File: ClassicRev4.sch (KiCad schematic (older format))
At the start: 60 parts, among them IC1 7805TV, IC2 MEGA8-P, IC3 74141N, Q1 IRF740, Q2 16MHz, Q3 2N7000, Q4 2N7000, Q5 2N7000, Q6 2N7000

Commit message: Initial commit Classic Rev4c
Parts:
- added TP4: HVD, Recovered:TESTPAD_P1-13, symbol TEST_1P
- IC3: value 74141N -> K155ID1
- SV2: footprint Recovered:ARDUNIX6_MA04-1 -> Recovered:ARDUNIX6_MA06-1; symbol ARDUNIX6_MA04-1 -> ARDUNIX6_MA06-1
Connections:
- net labels added: B_GATE, GPIO, G_GATE, PIR, R_GATE, TICK_BASE
- net labels removed: N$1, N$31, N$32, N$35, gnd
- wire segments 229 -> 231

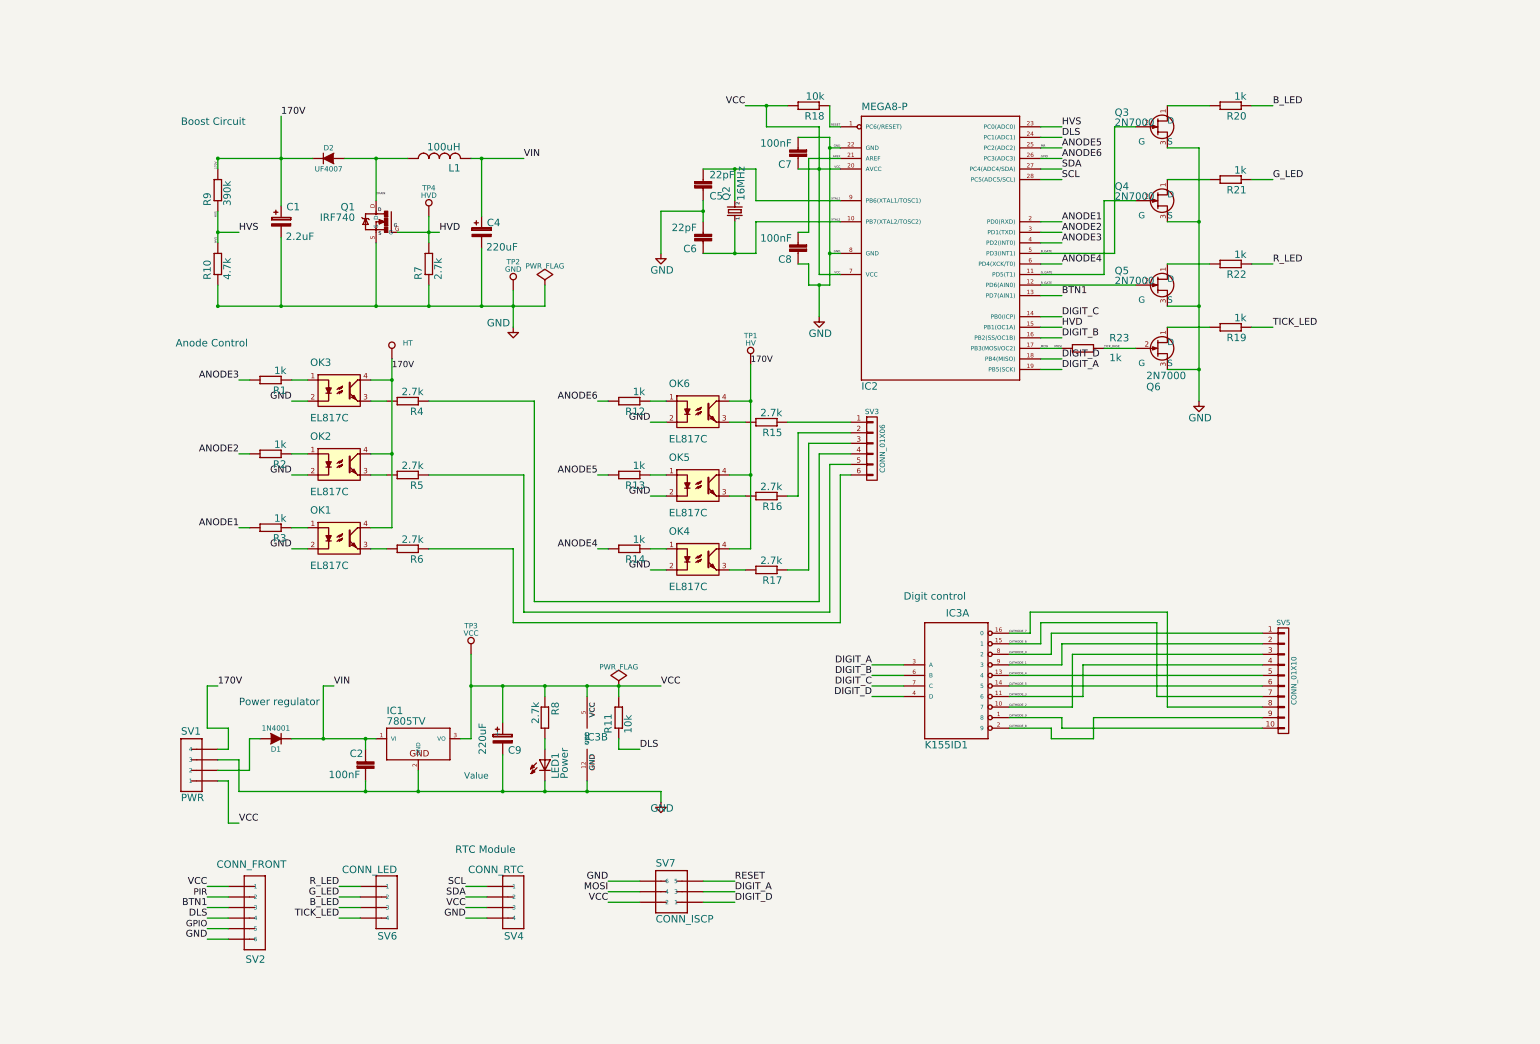
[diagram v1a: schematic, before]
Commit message: Correct values and divide more logically
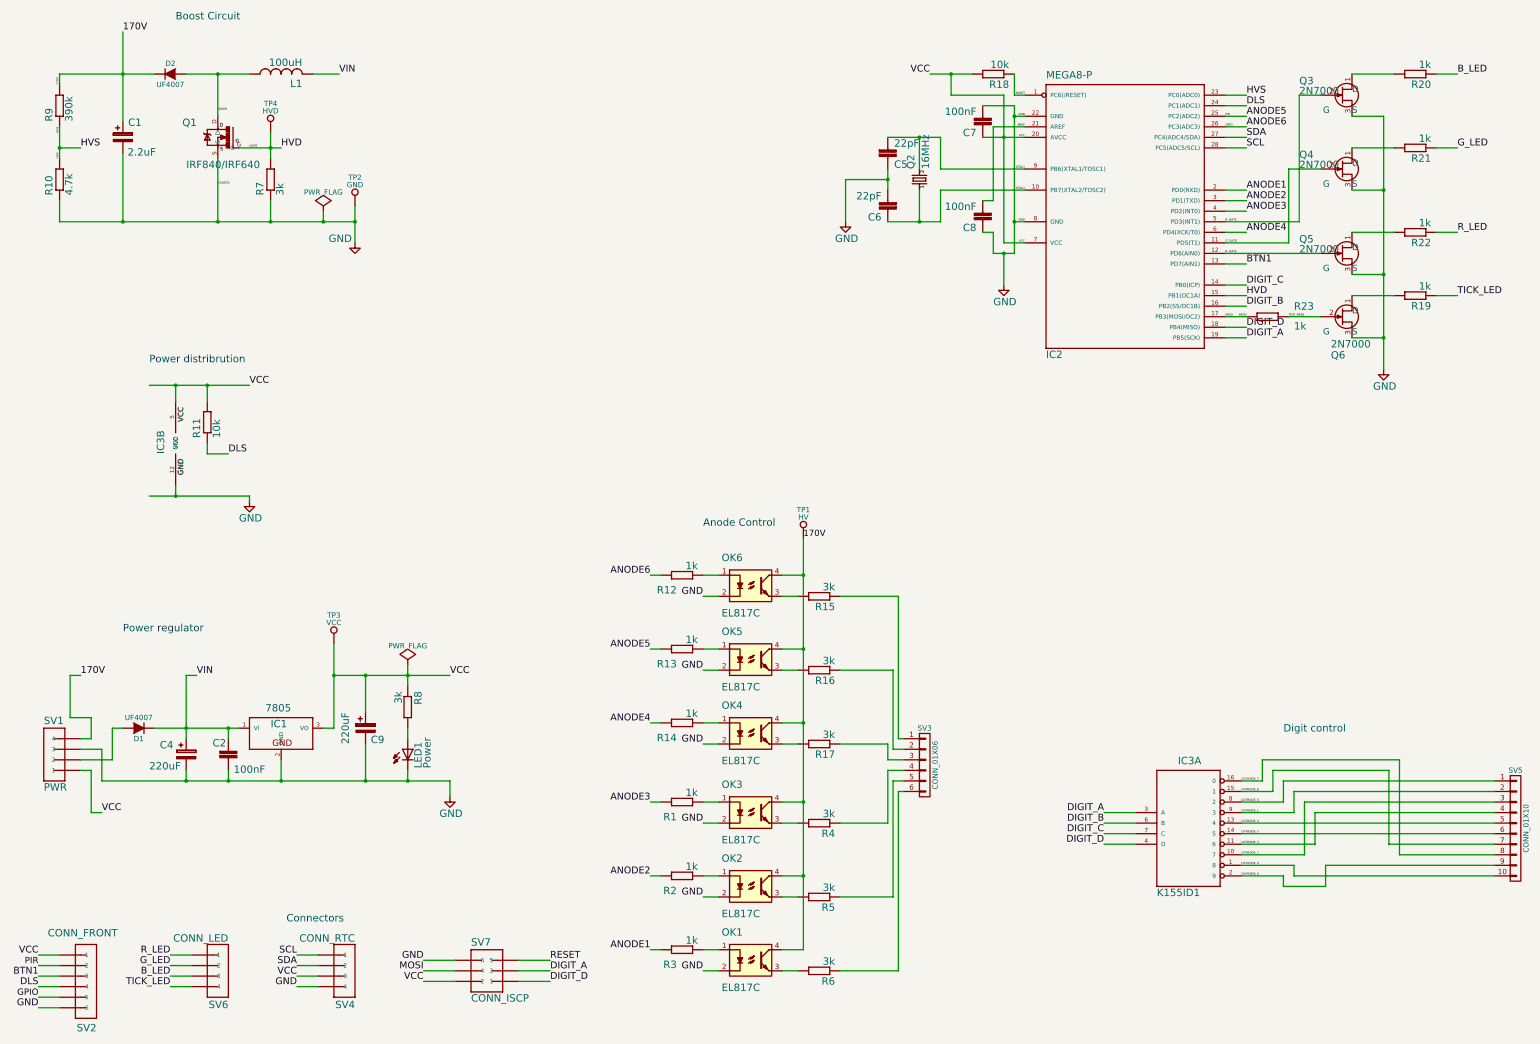
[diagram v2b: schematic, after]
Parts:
- D1: value 1N4001 -> UF4007
- IC1: value 7805TV -> 7805
- Q1: value IRF740 -> IRF840/IRF640
- R15, R16, R17, R4, R5, R6, R7, R8: value 2.7k -> 3k
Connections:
- net HVD renamed GATE
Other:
- note added: "Connectors"
- note added: "Power distribrution"
- note removed: "RTC Module"
- moved on the sheet: C1, C2, C4, C5, C6, C7, C8, C9, D1, D2, IC1, IC2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

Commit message: KiCad 5
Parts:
- C1, C4, C9: symbol CP -> ClassicRev4-rescue:CP
- C2, C5, C6, C7, C8: symbol RCL_C-EU050-024X044 -> ClassicRev4:RCL_C-EU050-024X044
- D1, D2: symbol D -> ClassicRev4-rescue:D
- IC1: symbol LINEAR_7805TV -> ClassicRev4:LINEAR_7805TV
- IC2: symbol ATMEL_MEGA8-P -> ClassicRev4:ATMEL_MEGA8-P
- IC3: symbol 74XX-US_74141N -> ClassicRev4:74XX-US_74141N
- L1: symbol RCL_L-US6000-XXX-RC -> ClassicRev4:RCL_L-US6000-XXX-RC
- LED1: symbol LED_LED3MM -> ClassicRev4:LED_LED3MM
- OK1, OK2, OK3, OK4, OK5, OK6: symbol PC817 -> ClassicRev4-rescue:PC817
- Q1: symbol IRF740 -> ClassicRev4-rescue:IRF740
- Q2: symbol CRYSTAL_CRYSTALHC49S -> ClassicRev4:CRYSTAL_CRYSTALHC49S
- Q3, Q4, Q5, Q6: symbol Q_NJFET_DGS -> ClassicRev4-rescue:Q_NJFET_DGS
- R1, R10, R11, R12, R13, R14, R15, R16, R17, R18, R19, R2, R20, R21, R22, R23, R3, R4, R5, R6, R7, R8, R9: symbol RCL_R-EU_0207/2V -> ClassicRev4-rescue:RCL_R-EU_0207_2V
- SV1, SV4, SV6: symbol ARDUNIX6_MA04-1 -> ClassicRev4:ARDUNIX6_MA04-1
- SV2: symbol ARDUNIX6_MA06-1 -> ClassicRev4:ARDUNIX6_MA06-1
- SV3: symbol CONN_01X06 -> ClassicRev4-rescue:CONN_01X06
- SV5: symbol CONN_01X10 -> ClassicRev4-rescue:CONN_01X10
- SV7: symbol CON-LSTB_MA03-2 -> ClassicRev4:CON-LSTB_MA03-2
- TP1, TP2, TP3, TP4: symbol TEST_1P -> ClassicRev4-rescue:TEST_1P

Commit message: Set voltage
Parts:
- C1: value 2.2uF -> 2.2uF 400V
- C4: value 220uF -> 220uF 16V
- C9: value 220uF -> 220uF 10V
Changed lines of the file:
@@
 P 2800 8050
 F 0 "C4" H 2550 8100 70  0000 L BNN
-F 1 "220uF" H 2450 7900 70  0000 L BNN
+F 1 "220uF 16V" H 2450 7900 70  0000 L BNN
 F 2 "rcl:rcl-E2,5-7" H 2790 7840 70  0001 L TNN
 F 3 "" H 2800 8050 60  0001 C CNN
@@
 P 4500 7800
 F 0 "C9" H 4550 7650 70  0000 L BNN
-F 1 "220uF" V 4350 7650 70  0000 L BNN
+F 1 "220uF 10V" V 4350 7650 70  0000 L BNN
 F 2 "rcl:rcl-E2,5-7" H 4490 7590 70  0001 L TNN
 F 3 "" H 4500 7800 60  0001 C CNN
@@
 P 2200 2200
 F 0 "C1" H 2250 2300 70  0000 L BNN
-F 1 "2.2uF" H 2244 2019 70  0000 L BNN
+F 1 "2.2uF 400V" H 2244 2019 70  0000 L BNN
 F 2 "rcl:rcl-E2,5-7" H 2190 1990 70  0001 L TNN
 F 3 "" H 2200 2200 60  0001 C CNN
